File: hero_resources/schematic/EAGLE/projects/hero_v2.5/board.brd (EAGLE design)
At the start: 61.1 x 61.1 mm, 43 parts, among them IC1 TP4056, IC2 4051D

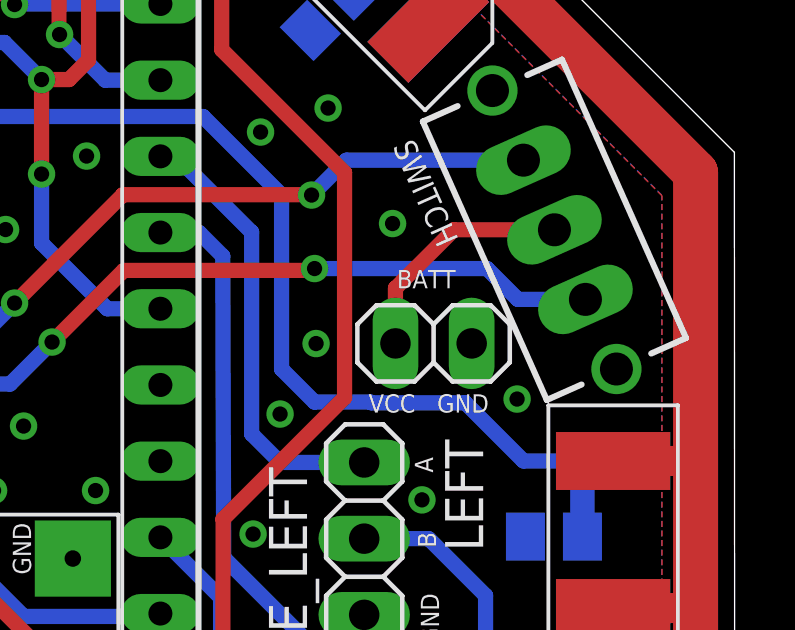
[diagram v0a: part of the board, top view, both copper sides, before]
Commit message: Fix battery connector position in board v2.5
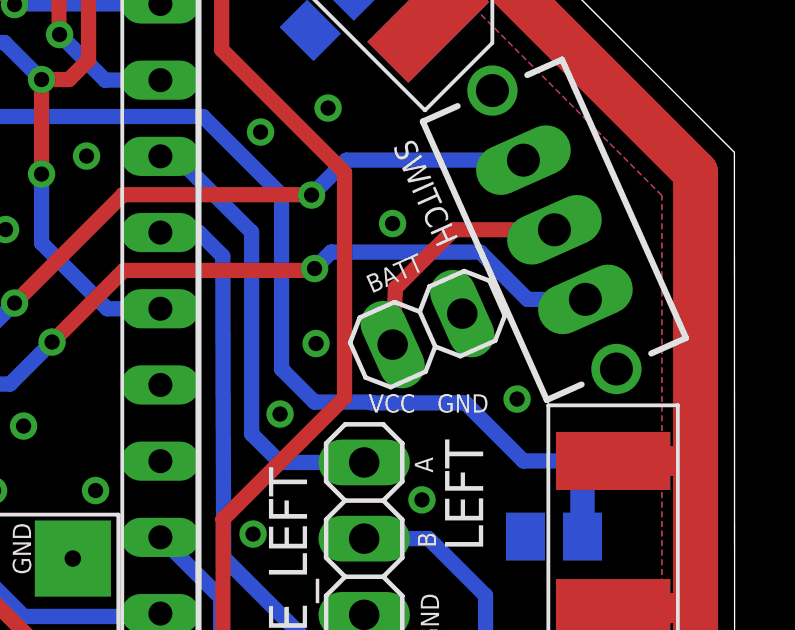
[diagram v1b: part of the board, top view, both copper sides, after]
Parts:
- moved BATT 0.52 mm to (32.5, 36.5), turned to 204 degrees
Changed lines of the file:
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@@
 <drawing>
 <settings>
-<setting alwaysvectorfont="no"/>
+<setting alwaysvectorfont="yes"/>
 <setting verticaltext="up"/>
 </settings>
@@
 </layers>
 <board>
-<fusionsync huburn="a.cGVyc29uYWw6dWUyYWU5Yjc4" projecturn="a.cGVyc29uYWw6dWUyYWU5Yjc4IzIwMTgwODExMTQzNTk5Njc2" f3durn="urn:adsk.wipprod:dm.lineage:RdjoPunqS2qz4CF9KvcqZg" pcbguid="0393263e-a8aa-4ff3-9bb2-e8f0add2bc9f" lastpulledtime="" lastsyncedchangeguid="45ac4ad0-f076-54e5-ce69-0c6a4673556f"/>
+<fusionsync huburn="a.cGVyc29uYWw6dWUyYWU5Yjc4" projecturn="a.cGVyc29uYWw6dWUyYWU5Yjc4IzIwMTgwODExMTQzNTk5Njc2" f3durn="urn:adsk.wipprod:dm.lineage:KWYvRUArSgWObtkZmYWDFg" pcbguid="f618bd25-d99b-4126-aee0-2615e3f46cf6" lastpulledtime="" lastsyncedchangeguid="65fcbdeb-8237-ccf0-1746-306a4b106965"/>
 <plain>
 <wire x1="42.744209375" y1="42.375221875" x2="25.088571875" y2="60.0071" width="0" layer="20"/>
@@
 </element>
 <element name="OS1" library="stepup" package="STEPUP" value="" x="12.20838125" y="20.299340625" smashed="yes" rot="R90"/>
-<element name="BATT" library="pinhead" library_urn="urn:adsk.eagle:library:325" package="1X02" package3d_urn="urn:adsk.eagle:package:22435/2" value="" x="32.7167" y="36.0056" smashed="yes" rot="R180">
-<attribute name="NAME" x="31.4949" y="37.8425" size="0.6096" layer="25" font="vector"/>
+<element name="BATT" library="pinhead" library_urn="urn:adsk.eagle:library:325" package="1X02" package3d_urn="urn:adsk.eagle:package:22435/2" value="" x="32.51370625" y="36.481434375" smashed="yes" rot="R204">
+<attribute name="NAME" x="30.6504" y="37.662575" size="0.6096" layer="25" font="vector" rot="R24"/>
 </element>
 <element name="C1" library="adafruit" library_urn="urn:adsk.eagle:library:420" package="C0603" package3d_urn="urn:adsk.eagle:package:6240338/1" value="0.10 nF" x="10.5791" y="44.4119" smashed="yes" rot="MR180">
@@
 <element name="IC1" library="TP4056" package="SOP-8" value="TP4056" x="13.85" y="40.2" smashed="yes" rot="R270">
 <attribute name="NAME" x="16.24" y="41.61" size="1.27" layer="25" rot="R270"/>
+<attribute name="SPICEPREFIX" value="X" x="13.85" y="40.2" size="1.778" layer="27" rot="R270" display="off"/>
 </element>
 <element name="R12" library="resistor" library_urn="urn:adsk.eagle:library:348" package="R0603" package3d_urn="urn:adsk.eagle:package:23555/3" value="102" x="17.832840625" y="4.90858125" smashed="yes" rot="R270">
@@
 <wire x1="18.6" y1="34.65" x2="15.75" y2="34.65" width="0.508" layer="16"/>
 <contactref element="SWITCH" pad="1"/>
-<wire x1="37.778378125" y1="37.472309375" x2="35.527690625" y2="37.472309375" width="0.508" layer="16"/>
-<wire x1="35.527690625" y1="37.472309375" x2="34.5" y2="38.5" width="0.508" layer="16"/>
-<wire x1="34.5" y1="38.5" x2="28.75" y2="38.5" width="0.508" layer="16"/>
+<wire x1="37.778378125" y1="37.472309375" x2="35.847690625" y2="37.472309375" width="0.508" layer="16"/>
+<wire x1="35.847690625" y1="37.472309375" x2="34.27" y2="39.05" width="0.508" layer="16"/>
+<wire x1="34.27" y1="39.05" x2="29.3" y2="39.05" width="0.508" layer="16"/>
+<wire x1="29.3" y1="39.05" x2="28.75" y2="38.5" width="0.508" layer="16"/>
 <wire x1="15.75" y1="34.65" x2="15.75" y2="37.445" width="0.508" layer="1"/>
 <wire x1="15.75" y1="37.445" x2="15.755" y2="37.45" width="0.508" layer="1"/>
@@
 <contactref element="BATT" pad="2"/>
 <contactref element="SWITCH" pad="2"/>
-<wire x1="31.4467" y1="36.0056" x2="31.4467" y2="37.8467" width="0.508" layer="1"/>
+<wire x1="31.353503125" y1="35.964878125" x2="31.4467" y2="37.8467" width="0.508" layer="1"/>
 <wire x1="33.392715625" y1="39.792715625" x2="36.74526875" y2="39.792715625" width="0.508" layer="1"/>
 <wire x1="31.4467" y1="37.8467" x2="33.392715625" y2="39.792715625" width="0.508" layer="1"/>
@@
 </signals>
 <mfgpreviewcolors>
-<mfgpreviewcolor name="soldermaskcolor" color="0xC8008000"/>
-<mfgpreviewcolor name="silkscreencolor" color="0xFFFEFEFE"/>
+<mfgpreviewcolor name="soldermaskcolor" color="0xC8D8D8D8"/>
+<mfgpreviewcolor name="silkscreencolor" color="0xFF3E3E3E"/>
 <mfgpreviewcolor name="backgroundcolor" color="0xFF282828"/>
 <mfgpreviewcolor name="coppercolor" color="0xFFFFBF00"/>

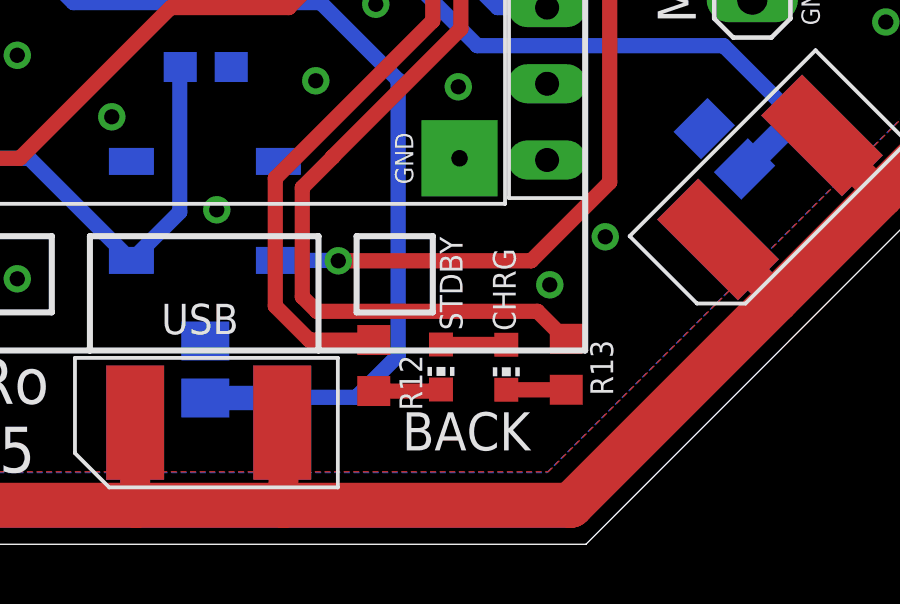
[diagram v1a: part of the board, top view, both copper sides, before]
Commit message: Fix board v2.5 charge power led to 0805.
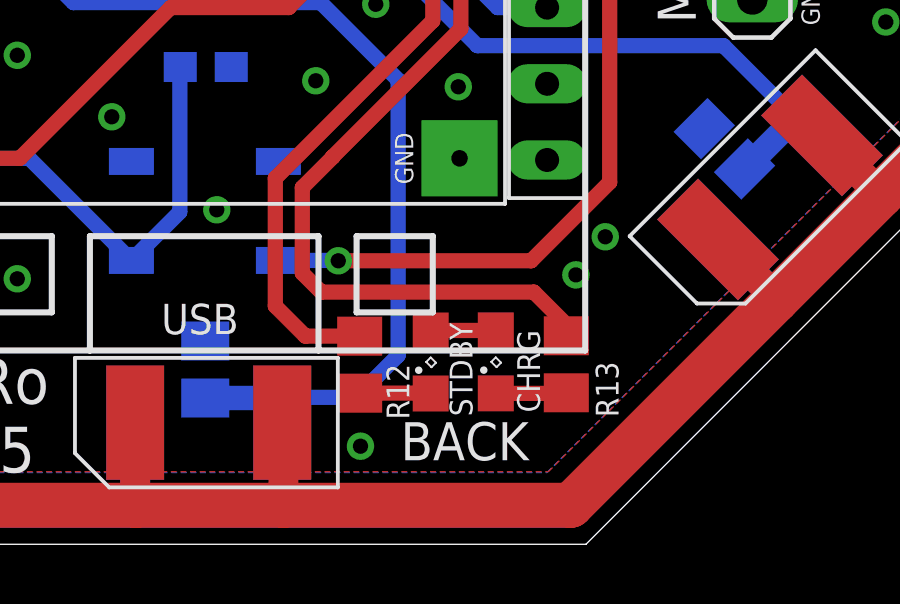
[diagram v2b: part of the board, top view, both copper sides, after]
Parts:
- CHRG, STDBY: device led:CHIP-LED0603 -> led:SML0805
- R12, R13: device resistor:R0603 -> resistor:R0805
- moved R12 0.47 mm to (17.4, 4.94)
- moved CHRG 0.39 mm to (21.9, 5.03), turned to 90 degrees
- moved STDBY 0.38 mm to (19.7, 5.03), turned to 90 degrees
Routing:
- net CHRG: track 44.4 -> 43.8 mm
- net STDBY: track 39.2 -> 38.7 mm
- net GND: vias 57 -> 58
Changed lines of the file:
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@@
 <drawing>
 <settings>
-<setting alwaysvectorfont="yes"/>
+<setting alwaysvectorfont="no"/>
 <setting verticaltext="up"/>
 </settings>
@@
 <wire x1="42.754734375" y1="16.808825" x2="42.744209375" y2="42.375221875" width="0" layer="20"/>
 <text x="23.35" y="54.95" size="1.27" layer="26" rot="MR0">FRONT</text>
-<text x="23.1" y="2.1" size="1.27" layer="26" rot="MR0">BACK</text>
+<text x="22.96" y="1.75" size="1.27" layer="26" rot="MR0">BACK</text>
 <text x="6.6" y="19.65" size="0.6096" layer="26" rot="MR180">SCL     SDA
 TX       RX     </text>
@@
 <text x="4.49" y="3.25" size="1.524" layer="25" rot="R180" align="center">HeRo
 v2.5</text>
-<text x="23.05" y="3.35" size="1.27" layer="25" rot="R180">BACK</text>
+<text x="23" y="3.02" size="1.27" layer="25" rot="R180">BACK</text>
 <text x="23.25" y="56.2" size="1.27" layer="25" rot="R180">FRONT</text>
 <text x="-9.9" y="32.65" size="1.27" layer="25" rot="R270">RIGHT</text>
@@
 <attribute name="SPICEPREFIX" value="X" x="13.85" y="40.2" size="1.778" layer="27" rot="R270" display="off"/>
 </element>
-<element name="R12" library="resistor" library_urn="urn:adsk.eagle:library:348" package="R0603" package3d_urn="urn:adsk.eagle:package:23555/3" value="102" x="17.832840625" y="4.90858125" smashed="yes" rot="R270">
-<attribute name="NAME" x="18.68843125" y="5.260653125" size="0.762" layer="25" rot="R270"/>
-<attribute name="VALUE" x="14.911840625" y="7.06758125" size="1.27" layer="27" rot="R270"/>
-</element>
-<element name="R13" library="resistor" library_urn="urn:adsk.eagle:library:348" package="R0603" package3d_urn="urn:adsk.eagle:package:23555/3" value="102" x="24.25" y="4.95" smashed="yes" rot="R270">
-<attribute name="NAME" x="25.051" y="5.759" size="0.762" layer="25" rot="R270"/>
+<element name="R12" library="resistor" library_urn="urn:adsk.eagle:library:348" package="R0805" package3d_urn="urn:adsk.eagle:package:23553/2" value="102" x="17.362840625" y="4.93858125" smashed="yes" rot="R270">
+<attribute name="NAME" x="18.25843125" y="4.960653125" size="0.762" layer="25" rot="R270"/>
+<attribute name="VALUE" x="14.441840625" y="7.09758125" size="1.27" layer="27" rot="R270"/>
+</element>
+<element name="R13" library="resistor" library_urn="urn:adsk.eagle:library:348" package="R0805" package3d_urn="urn:adsk.eagle:package:23553/2" value="102" x="24.25" y="4.95" smashed="yes" rot="R270">
+<attribute name="NAME" x="25.231" y="5.039" size="0.762" layer="25" rot="R270"/>
 <attribute name="VALUE" x="21.329" y="7.109" size="1.27" layer="27" rot="R270"/>
 </element>
@@
 <attribute name="VALUE" x="13.663" y="44.78" size="1.27" layer="27" rot="R90"/>
 </element>
-<element name="STDBY" library="led" library_urn="urn:adsk.eagle:library:259" package="CHIP-LED0603" package3d_urn="urn:adsk.eagle:package:15819/3" value="" x="20.07321875" y="4.861090625" smashed="yes" rot="R180">
-<attribute name="NAME" x="20.794284375" y="6.08718125" size="0.762" layer="25" rot="R90"/>
-<attribute name="VALUE" x="18.16821875" y="5.4960875" size="1.27" layer="27" rot="R270"/>
-</element>
-<element name="CHRG" library="led" library_urn="urn:adsk.eagle:library:259" package="CHIP-LED0603" package3d_urn="urn:adsk.eagle:package:15819/3" value="" x="22.25" y="4.85" smashed="yes" rot="R180">
-<attribute name="NAME" x="22.565" y="6.065" size="0.762" layer="25" rot="R90"/>
-<attribute name="VALUE" x="20.345" y="5.485" size="1.27" layer="27" rot="R270"/>
+<element name="STDBY" library="led" library_urn="urn:adsk.eagle:library:259" package="SML0805" package3d_urn="urn:adsk.eagle:package:15830/1" value="" x="19.731090625" y="5.02678125" smashed="yes" rot="R90">
+<attribute name="NAME" x="21.124284375" y="3.21718125" size="0.762" layer="25" rot="R90"/>
+<attribute name="VALUE" x="20.3660875" y="6.93178125" size="1.27" layer="27" rot="R180"/>
+</element>
+<element name="CHRG" library="led" library_urn="urn:adsk.eagle:library:259" package="SML0805" package3d_urn="urn:adsk.eagle:package:15830/1" value="" x="21.9" y="5.03" smashed="yes" rot="R90">
+<attribute name="NAME" x="23.375" y="3.345" size="0.762" layer="25" rot="R90"/>
+<attribute name="VALUE" x="22.535" y="6.935" size="1.27" layer="27" rot="R180"/>
 </element>
 <element name="SWITCH" library="switch" library_urn="urn:adsk.eagle:library:380" package="TL3XYO" package3d_urn="urn:adsk.eagle:package:27747/1" value="TL37YO" x="36.74526875" y="39.792715625" smashed="yes" rot="R114">
@@
 <via x="12.55" y="18.1" extent="1-16" drill="0.508"/>
 <via x="20.65" y="14.2" extent="1-16" drill="0.508"/>
-<via x="23.7" y="7.6" extent="1-16" drill="0.508"/>
+<via x="24.57" y="7.93" extent="1-16" drill="0.508"/>
 <via x="25.55" y="9.2" extent="1-16" drill="0.508"/>
 <via x="5.95" y="15.25" extent="1-16" drill="0.508"/>
@@
 <contactref element="IRLML2502" pad="2"/>
 <via x="4.92" y="34.57" extent="1-16" drill="0.508"/>
+<via x="17.39" y="2.22" extent="1-16" drill="0.508"/>
 </signal>
 <signal name="VCC">
@@
 <wire x1="19.8" y1="16.4" x2="14.55" y2="11.15" width="0.508" layer="1"/>
 <wire x1="14.55" y1="11.15" x2="14.55" y2="6.891421875" width="0.508" layer="1"/>
-<wire x1="15.682840625" y1="5.75858125" x2="17.832840625" y2="5.75858125" width="0.508" layer="1"/>
-<wire x1="14.55" y1="6.891421875" x2="15.682840625" y2="5.75858125" width="0.508" layer="1"/>
+<wire x1="15.552840625" y1="5.88858125" x2="14.55" y2="6.891421875" width="0.508" layer="1"/>
+<wire x1="17.362840625" y1="5.88858125" x2="15.552840625" y2="5.88858125" width="0.508" layer="1"/>
 </signal>
 <signal name="CHRG">
@@
 <wire x1="20.7356" y1="24.7144" x2="20.7356" y2="16.1356" width="0.508" layer="1"/>
 <wire x1="16.46120625" y1="11.86120625" x2="20.7356" y2="16.1356" width="0.508" layer="1"/>
-<wire x1="15.45" y1="7.2" x2="15.934221875" y2="6.715778125" width="0.508" layer="1"/>
-<wire x1="15.45" y1="7.2" x2="15.45" y2="10.83879375" width="0.508" layer="1"/>
+<wire x1="15.45" y1="7.99" x2="16.084221875" y2="7.355778125" width="0.508" layer="1"/>
+<wire x1="15.45" y1="7.99" x2="15.45" y2="10.83879375" width="0.508" layer="1"/>
 <wire x1="15.45" y1="10.83879375" x2="16.4724125" y2="11.86120625" width="0.508" layer="1"/>
 <wire x1="16.4724125" y1="11.86120625" x2="16.46120625" y2="11.86120625" width="0.508" layer="1"/>
-<wire x1="15.934221875" y1="6.715778125" x2="23.291059375" y2="6.715778125" width="0.508" layer="1"/>
-<wire x1="24.2068375" y1="5.8" x2="24.25" y2="5.8" width="0.508" layer="1"/>
-<wire x1="23.291059375" y1="6.715778125" x2="24.2068375" y2="5.8" width="0.508" layer="1"/>
+<wire x1="16.084221875" y1="7.355778125" x2="23.171059375" y2="7.355778125" width="0.508" layer="1"/>
+<wire x1="24.25" y1="6.2768375" x2="23.171059375" y2="7.355778125" width="0.508" layer="1"/>
+<wire x1="24.25" y1="6.2768375" x2="24.25" y2="5.9" width="0" layer="19" extent="1-1"/>
 </signal>
 <signal name="PROG">
@@
 <contactref element="R13" pad="2"/>
 <contactref element="CHRG" pad="C"/>
-<wire x1="22.25" y1="4.1" x2="24.25" y2="4.1" width="0.508" layer="1"/>
+<wire x1="21.9" y1="3.98" x2="24.23" y2="3.98" width="0.508" layer="1"/>
+<wire x1="24.23" y1="3.98" x2="24.25" y2="4" width="0.508" layer="1"/>
 </signal>
 <signal name="N$8">
 <contactref element="R12" pad="2"/>
 <contactref element="STDBY" pad="C"/>
-<wire x1="17.832840625" y1="4.05858125" x2="20.020709375" y2="4.05858125" width="0.508" layer="1"/>
-<wire x1="20.020709375" y1="4.05858125" x2="20.07321875" y2="4.111090625" width="0.508" layer="1"/>
+<wire x1="17.362840625" y1="3.98858125" x2="19.719290625" y2="3.98858125" width="0.508" layer="1"/>
+<wire x1="19.719290625" y1="3.98858125" x2="19.731090625" y2="3.97678125" width="0.508" layer="1"/>
 </signal>
 <signal name="N$1">
 <contactref element="CHRG" pad="A"/>
 <contactref element="STDBY" pad="A"/>
-<wire x1="20.07321875" y1="5.611090625" x2="22.238909375" y2="5.611090625" width="0.508" layer="1"/>
-<wire x1="22.238909375" y1="5.611090625" x2="22.25" y2="5.6" width="0.508" layer="1"/>
+<wire x1="19.731090625" y1="6.07678125" x2="21.89678125" y2="6.07678125" width="0.508" layer="1"/>
+<wire x1="21.89678125" y1="6.07678125" x2="21.9" y2="6.08" width="0.508" layer="1"/>
 </signal>
 <signal name="TP_B+">
